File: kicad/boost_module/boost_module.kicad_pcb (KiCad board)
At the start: 2 copper layers, 35 parts, among them J1 Conn_01x02, J2 Conn_01x02, J3 Conn_01x02, U1 OPA1612AxD

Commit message: initial placement
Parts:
- removed C11, C12, C13: 22U, Capacitor_SMD:C_1210_3225Metric_Pad1.33x2.70mm_HandSolder
- removed C6: 10u, Capacitor_SMD:C_0603_1608Metric_Pad1.08x0.95mm_HandSolder
- removed R4: 100R, Resistor_SMD:R_0603_1608Metric_Pad0.98x0.95mm_HandSolder
- added U1: OPA188xxDBV, Package_TO_SOT_SMD:TSOT-23-5, F.Cu at (2.08, 1.73)
- U1: value OPA1612AxD -> OPA188xxDBV; footprint Package_SO:SOIC-8_3.9x4.9mm_P1.27mm -> Package_TO_SOT_SMD:TSOT-23-5
- moved C14 78.1 mm to (147.3, 67.3), turned to 0 degrees
- moved C15 78.0 mm to (147.3, 63.8), turned to 0 degrees
- moved J1 71.6 mm to (162.6, 58.4), turned to -90 degrees
- moved J3 70.8 mm to (162.6, 73.7), turned to -90 degrees
- moved D2 70.4 mm to (161.8, 63.2), turned to 0 degrees
- moved D1 69.9 mm to (161.8, 61.2), turned to 0 degrees
- moved R7 69.2 mm to (150.6, 60.2)
- moved C10 68.7 mm to (157.0, 70.1)
- moved U1 68.6 mm to (152.4, 64.3)
- moved D3 68.4 mm to (143.1, 70.6), turned to 180 degrees
- moved RV1 68.4 mm to (154.9, 73.7)
- moved D4 68.4 mm to (161.3, 70.6), turned to 0 degrees
- moved C8 68.3 mm to (143.5, 67.6), turned to 90 degrees
- moved R11 68.3 mm to (161.3, 68.3), turned to 0 degrees
- moved C9 67.8 mm to (153.2, 70.1)
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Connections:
- C5 pad 1: /bias+ -> /VBIAS
- R2 pad 2: /bias+ -> /VBIAS
- R3 pad 1: /bias+ -> /VBIAS
- U1 pad 1: /bias_out -> /boost_out
- U1 pad 2: /VBIAS -> GND
- U1 pad 3: /bias+ -> /boost+
- U1 pad 4: GND -> /boost-
- U1 pad 5: /boost+ -> VCC
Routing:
- added copper zone on B.Cu, net GND
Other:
- board outline added: 25.4 x 20.3 mm

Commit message: component selection
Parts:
- removed the U1 at (2.08, 1.73)
- added C6: 2u2, capacitors:C_0603_1608Metric, F.Cu at (153.2, 58.4)
- C1, C2, C4, C5, C8, C9: footprint Capacitor_SMD:C_0603_1608Metric_Pad1.08x0.95mm_HandSolder -> capacitors:C_0603_1608Metric
- C10, C7: footprint Capacitor_SMD:C_0603_1608Metric_Pad1.08x0.95mm_HandSolder -> capacitors:C_1206_3216Metric
- C14, C15: value 22U -> 22u; footprint Capacitor_SMD:C_1210_3225Metric_Pad1.33x2.70mm_HandSolder -> capacitors:C_1206_3216Metric
- C3: value 10u -> 2u2; footprint Capacitor_SMD:C_0603_1608Metric_Pad1.08x0.95mm_HandSolder -> capacitors:C_0603_1608Metric
- D1, D3, D4: value D_TVS -> 12V 1A; footprint Diode_SMD:D_0603_1608Metric_Pad1.05x0.95mm_HandSolder -> SOD:D_SOD-323
- D2: value D -> 40V 500mA; footprint Diode_SMD:D_0603_1608Metric_Pad1.05x0.95mm_HandSolder -> SOD:D_SOD-323
- R1, R10, R11, R2, R3, R5, R6, R7, R8, R9: footprint Resistor_SMD:R_0603_1608Metric_Pad0.98x0.95mm_HandSolder -> resistors:R_0603_1608Metric
- U1: value OPA188xxDBV -> OPA1677; footprint Package_TO_SOT_SMD:TSOT-23-5 -> SOT:TSOT-23-5
- moved R10 3.34 mm to (160.3, 68.1), turned to -90 degrees
- moved R5 3.06 mm to (144.5, 67.8)
- moved R6 2.70 mm to (144.3, 61.7), turned to 0 degrees
- moved J2 2.54 mm to (144.8, 73.7), turned to -90 degrees
- moved J3 2.54 mm to (160.0, 73.7), turned to 90 degrees
- moved C4 2.50 mm to (157.5, 65.0), turned to 0 degrees
- moved R2 2.41 mm to (149.4, 57.7)
- moved C15 1.98 mm to (148.8, 65.0)
- moved C7 1.98 mm to (148.8, 62.2)
- moved C5 1.70 mm to (145.8, 59.7)
- moved R3 1.70 mm to (145.8, 57.7)
- moved C14 1.61 mm to (148.8, 67.8)
- moved C10 1.61 mm to (157.5, 68.6), turned to 90 degrees
- moved R7 1.37 mm to (149.4, 59.7), turned to 180 degrees
- moved U1 1.30 mm to (153.7, 64.5)
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
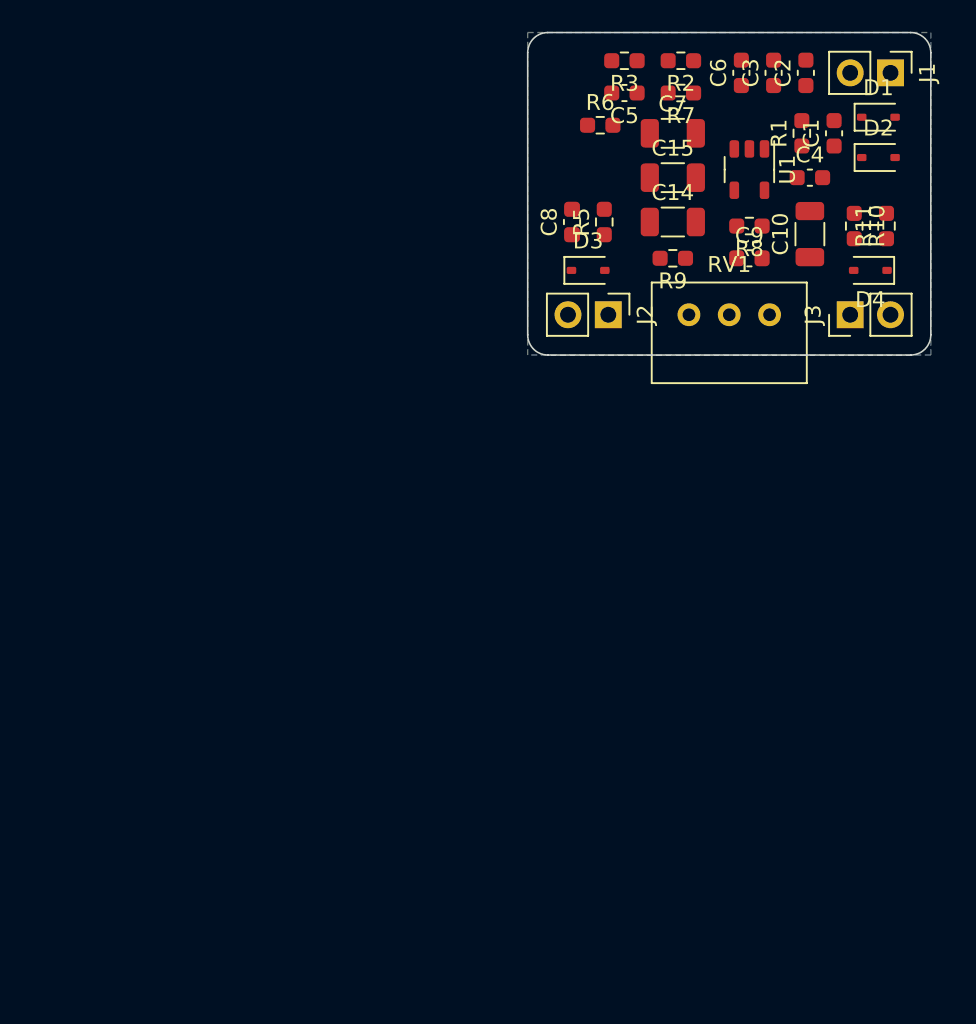
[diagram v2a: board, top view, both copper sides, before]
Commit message: added 1590G2 enclosure footprint
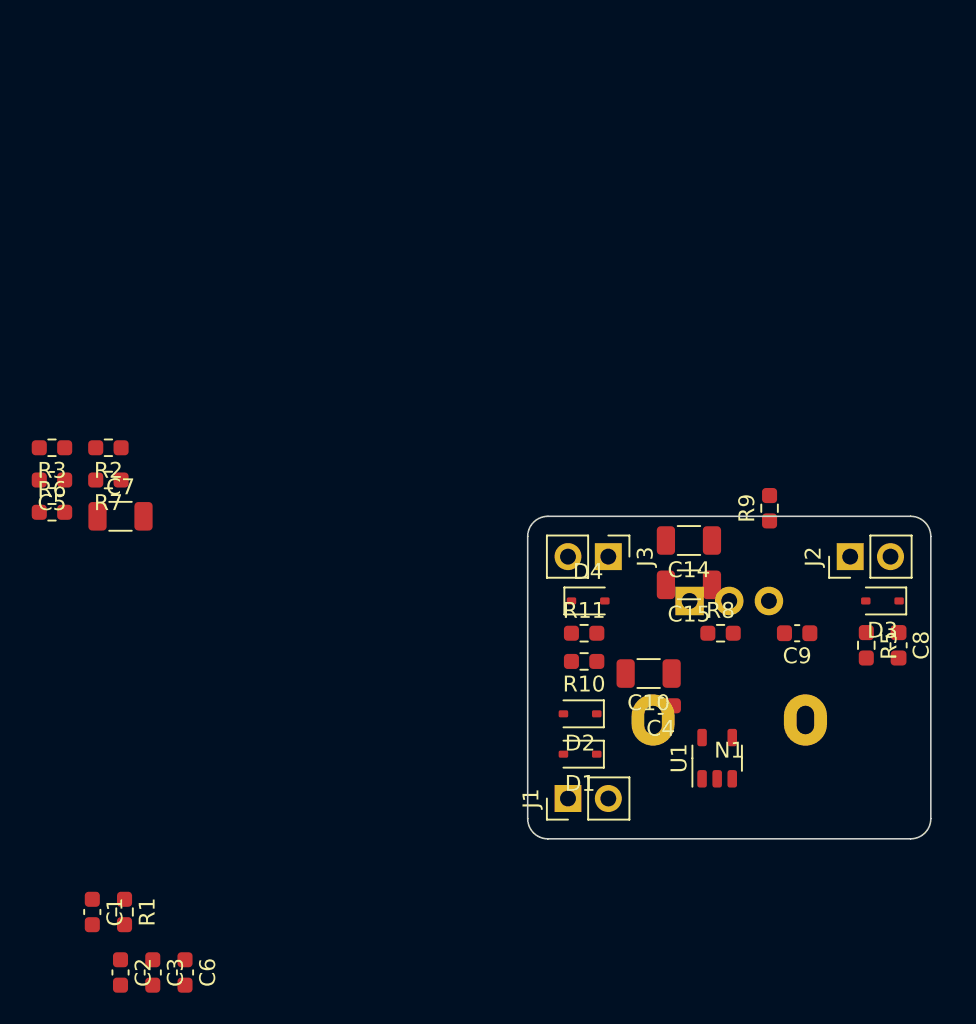
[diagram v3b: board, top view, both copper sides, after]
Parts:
- added N1: 1590G2, hammond:1590G, F.Cu at (152.4, 101.6)
- RV1: footprint Potentiometer_THT:Potentiometer_Bourns_3299W_Vertical -> potentiometers:Pot_RD901F-40-00D_Single_Vertical; moved to B.Cu
- moved C2 71.3 mm to (114.0, 115.1), turned to -90 degrees
- moved C3 68.9 mm to (116.1, 115.1), turned to -90 degrees
- moved C1 67.8 mm to (112.3, 111.3), turned to -90 degrees
- moved C6 66.6 mm to (118.1, 115.1), turned to -90 degrees
- moved R1 65.0 mm to (114.3, 111.3), turned to -90 degrees
- moved J1 50.0 mm to (142.2, 104.1), turned to 90 degrees
- moved D1 44.3 mm to (143.0, 101.3), turned to 180 degrees
- moved C5 43.5 mm to (109.7, 84.1)
- moved R2 43.5 mm to (113.3, 82.0)
- moved R3 43.5 mm to (109.7, 82.0)
- moved R7 43.5 mm to (113.3, 84.1)
- moved C7 42.3 mm to (114.0, 86.4)
- moved R6 42.3 mm to (109.7, 86.1)
- moved D2 39.8 mm to (143.0, 98.8), turned to 180 degrees
- moved U1 37.1 mm to (151.6, 101.6), turned to 90 degrees
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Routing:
- removed copper zone on B.Cu, net GND
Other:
- outline, holes or cut-outs redrawn

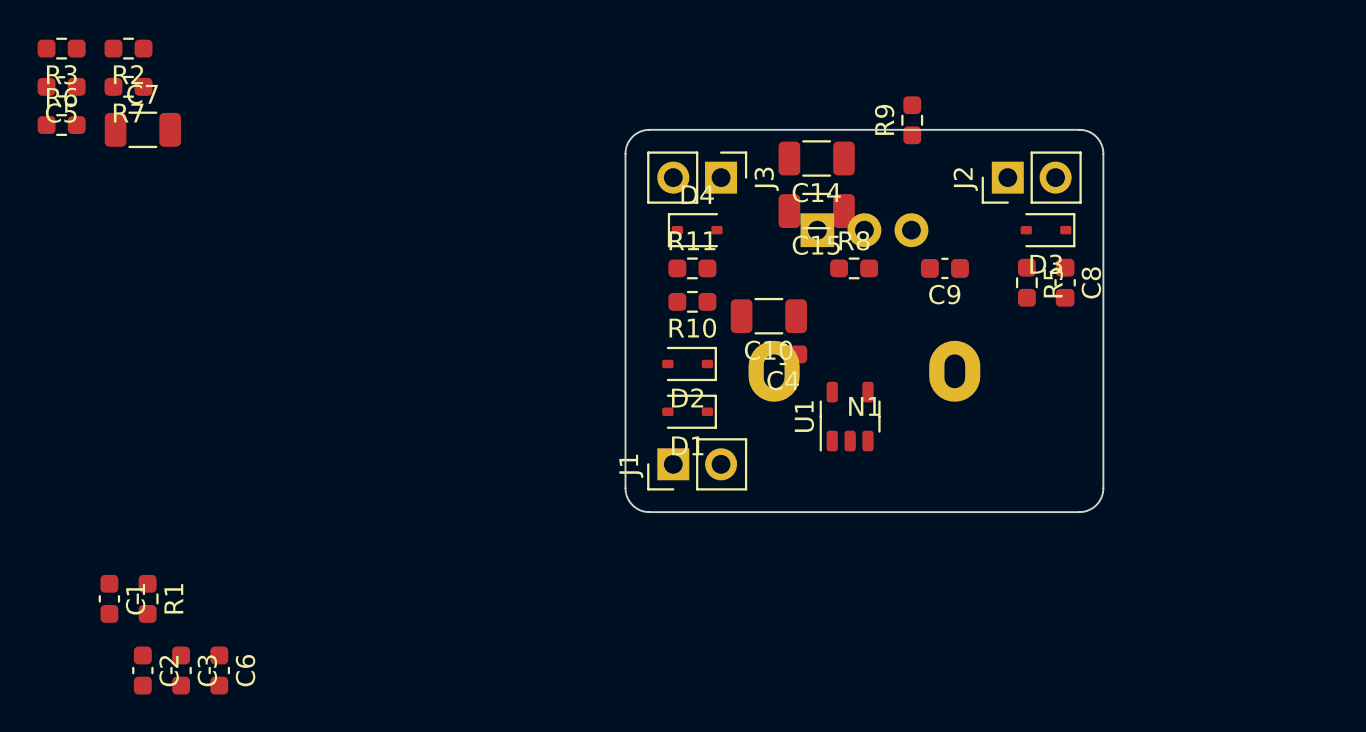
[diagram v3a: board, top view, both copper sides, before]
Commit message: changed layout for 1591XXLTBU enclosure
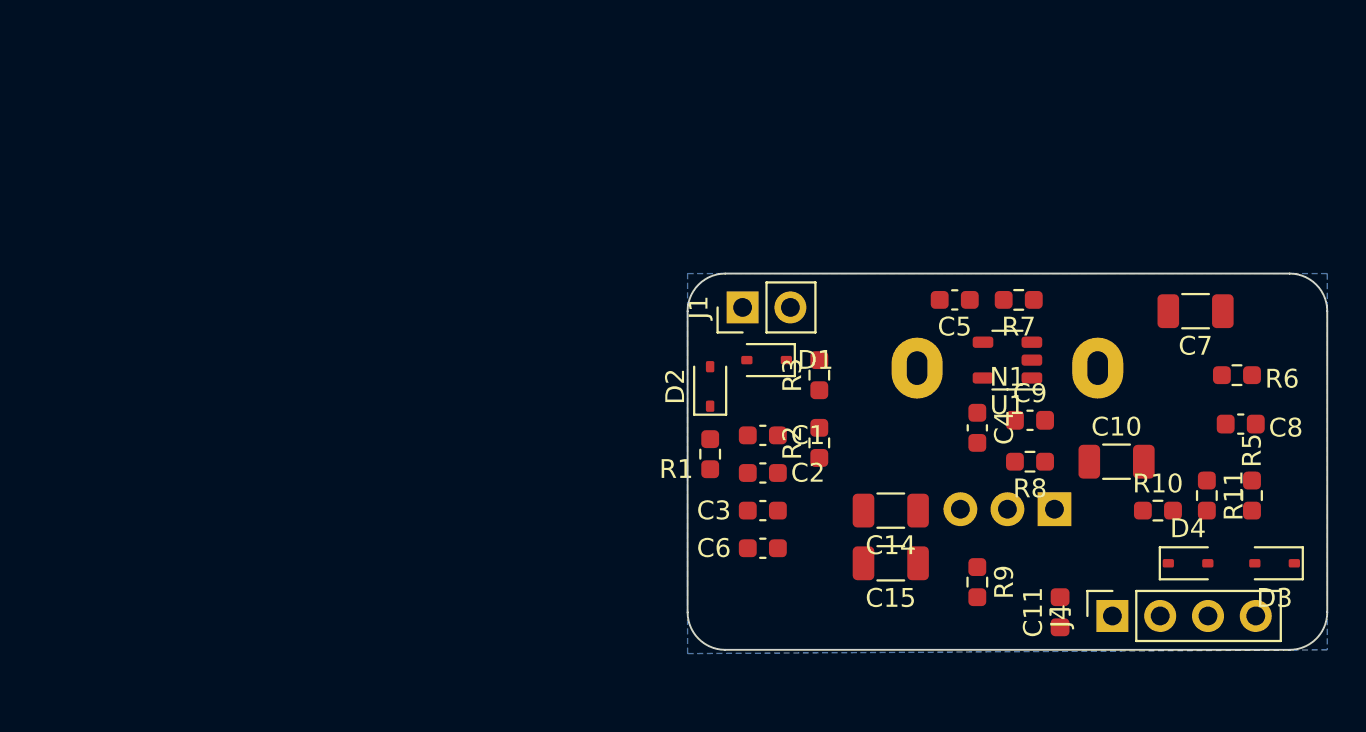
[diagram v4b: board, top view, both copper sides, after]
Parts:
- removed J2, J3: Conn_01x02, Connector_PinHeader_2.54mm:PinHeader_1x02_P2.54mm_Vertical
- added C11: 0u1, capacitors:C_0603_1608Metric, F.Cu at (162.8, 112.0)
- added J4: Conn_01x04, connectors_headers:PinSocket_1x04_P2.54mm_Vertical, F.Cu at (165.6, 112.2)
- moved R6 63.9 mm to (172.2, 99.4)
- moved C7 56.8 mm to (170.0, 96.0), turned to 180 degrees
- moved C5 48.8 mm to (157.2, 95.4)
- moved R7 48.7 mm to (160.6, 95.4)
- moved R3 43.9 mm to (150.0, 99.4), turned to 90 degrees
- moved R2 42.3 mm to (150.0, 103.0), turned to 90 degrees
- moved C1 35.8 mm to (147.0, 102.6), turned to 0 degrees
- moved C2 34.6 mm to (147.0, 104.6), turned to 0 degrees
- moved C3 32.1 mm to (147.0, 106.6), turned to 0 degrees
- moved D4 31.5 mm to (169.6, 109.4)
- moved R1 30.9 mm to (144.2, 103.6)
- moved R11 29.9 mm to (170.6, 105.8), turned to -90 degrees
- moved C6 29.6 mm to (147.0, 108.6), turned to 0 degrees
- moved R10 27.1 mm to (168.0, 106.6), turned to 0 degrees
- moved R9 24.8 mm to (158.4, 110.4), turned to -90 degrees
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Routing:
- added copper zone on B.Cu, net GND
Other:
- board size 25.4 x 20.3 mm -> 34 x 20 mm

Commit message: placement and routing
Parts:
- added TP1: TestPoint, TestPoint:TestPoint_Pad_D1.0mm, F.Cu at (148.8, 104.4)
- added TP2: TestPoint, TestPoint:TestPoint_Pad_D1.0mm, F.Cu at (148.8, 106.4)
- added TP3: TestPoint, TestPoint:TestPoint_Pad_D1.0mm, F.Cu at (159.7, 95.1)
- added TP4: TestPoint, TestPoint:TestPoint_Pad_D1.0mm, F.Cu at (168.1, 100.0)
- added TP5: TestPoint, TestPoint:TestPoint_Pad_D1.0mm, F.Cu at (163.7, 104.0)
- moved R2 8.55 mm to (157.8, 99.5)
- moved R3 8.22 mm to (157.8, 96.8), turned to 180 degrees
- moved D2 5.69 mm to (149.8, 101.0), turned to 0 degrees
- moved C7 5.29 mm to (172.0, 100.9)
- moved C2 5.20 mm to (145.0, 99.8), turned to 90 degrees
- moved J1 5.08 mm to (151.0, 96.0), turned to -90 degrees
- moved R8 4.62 mm to (160.8, 108.6)
- moved C5 4.52 mm to (161.5, 96.8), turned to 0 degrees
- moved R11 4.37 mm to (166.5, 107.3), turned to 0 degrees
- moved R6 3.95 mm to (172.8, 103.3)
- moved C6 3.77 mm to (145.0, 105.4), turned to -90 degrees
- moved C8 3.32 mm to (172.8, 105.3)
- moved R7 3.32 mm to (161.5, 98.6)
- moved C14 3.20 mm to (153.8, 109.8)
- moved D4 3.12 mm to (166.5, 109.4)
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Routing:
- net VCC: track 0.00 -> 41.0 mm
- net GND: track 0.00 -> 28.3 mm, vias 0 -> 11
- net /boost_out: track 0.00 -> 12.1 mm
- net /boost+: track 0.00 -> 11.4 mm
- net /boost-: track 0.00 -> 8.98 mm
- net /VBIAS: track 0.00 -> 7.83 mm
- net /in_filt: track 0.00 -> 7.48 mm
- net /out: track 0.00 -> 7.00 mm
- net Net-(C14-Pad1): track 0.00 -> 5.22 mm
- net /VCC_IN: track 0.00 -> 5.06 mm
- net /in: track 0.00 -> 5.03 mm
- net /VCC_FILT_IN: track 0.00 -> 4.00 mm
- net Net-(C10-Pad2): track 0.00 -> 2.50 mm
- net Net-(R9-Pad1): track 0.00 -> 2.07 mm
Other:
- rule pad_to_mask_clearance: 0 -> 0.0508
- board text added: "+"
- board text added: "-"
- board text added: "BOOST v0"
- board text added: "BST"
- board text added: "BST_IN"
- board text added: "GND"
- board text added: "OP AMP"
- board text added: "VBIAS"
- board text added: "VCC"
- board text added: "peterp145"
